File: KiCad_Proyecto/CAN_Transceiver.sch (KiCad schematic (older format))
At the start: 24 parts, among them Q6 2N7002, U4 MCP25612FD, U5 TH8056, U6 PESD1CAN, U7 PESD1CAN, U8 PESD1CAN

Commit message: todos los .sch arreglados
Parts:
- C16, C17, C18, C19, C20, C21, C22, C23: symbol PF_apiner-rescue:C-OBDII_IoT1 -> OBDII_IoT:C
- Q6: symbol PF_apiner-rescue:MOS_N-OBDII_IoT1 -> OBDII_IoT:MOS_N
- R15, R16, R17, R18, R19, R20, R21, R22, R23, R24: symbol PF_apiner-rescue:R-OBDII_IoT1 -> OBDII_IoT:R
- U4: symbol PF_apiner-rescue:MCP25612FD-OBDII_IoT1 -> OBDII_IoT:MCP25612FD
- U5: symbol PF_apiner-rescue:TH8056-OBDII_IoT1 -> OBDII_IoT:TH8056
- U6, U7, U8: symbol PF_apiner-rescue:PESD1CAN-OBDII_IoT1 -> OBDII_IoT:PESD1CAN
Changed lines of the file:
@@
 EESchema Schematic File Version 4
 LIBS:PF_apiner-cache
-EELAYER 29 0
+EELAYER 26 0
 EELAYER END
 $Descr A4 11693 8268
@@
 HS_CAN_RX
 $Comp
-L PF_apiner-rescue:PESD1CAN-OBDII_IoT1 U6
+L OBDII_IoT:PESD1CAN U6
 U 1 1 582F34D6
 P 5300 6250
@@
 $EndComp
 $Comp
-L PF_apiner-rescue:GND-OBDII_IoT1 #PWR060
+L OBDII_IoT:GND #PWR060
 U 1 1 582F433E
 P 5300 6700
@@
 $EndComp
 $Comp
-L PF_apiner-rescue:R-OBDII_IoT1 R21
+L OBDII_IoT:R R21
 U 1 1 58B0A852
 P 5750 5100
@@
 $EndComp
 $Comp
-L PF_apiner-rescue:MCP25612FD-OBDII_IoT1 U4
+L OBDII_IoT:MCP25612FD U4
 U 1 1 58EEA34D
 P 3450 5150
@@
 $EndComp
 $Comp
-L PF_apiner-rescue:TH8056-OBDII_IoT1 U5
+L OBDII_IoT:TH8056 U5
 U 1 1 58F03C6E
 P 3700 2950
@@
 SW_CAN_LOAD
 $Comp
-L PF_apiner-rescue:+5V_SW-OBDII_IoT1 #PWR061
+L OBDII_IoT:+5V_SW #PWR061
 U 1 1 58FD2521
 P 3150 5100
@@
 $EndComp
 $Comp
-L PF_apiner-rescue:PESD1CAN-OBDII_IoT1 U7
+L OBDII_IoT:PESD1CAN U7
 U 1 1 58FD2706
 P 6000 3650
@@
 $EndComp
 $Comp
-L PF_apiner-rescue:GND-OBDII_IoT1 #PWR062
+L OBDII_IoT:GND #PWR062
 U 1 1 58FD270C
 P 6000 4050
@@
 $EndComp
 $Comp
-L PF_apiner-rescue:R-OBDII_IoT1 R17
+L OBDII_IoT:R R17
 U 1 1 58FD347C
 P 4600 6100
@@
 $EndComp
 $Comp
-L PF_apiner-rescue:C-OBDII_IoT1 C19
+L OBDII_IoT:C C19
 U 1 1 58FD3B6F
 P 4600 6450
@@
 $EndComp
 $Comp
-L PF_apiner-rescue:R-OBDII_IoT1 R19
+L OBDII_IoT:R R19
 U 1 1 58FD3FA7
 P 4900 6100
@@
 $EndComp
 $Comp
-L PF_apiner-rescue:C-OBDII_IoT1 C20
+L OBDII_IoT:C C20
 U 1 1 58FD3FB1
 P 4900 6450
@@
 $EndComp
 $Comp
-L PF_apiner-rescue:PESD1CAN-OBDII_IoT1 U8
+L OBDII_IoT:PESD1CAN U8
 U 1 1 58FD4234
 P 6450 6250
@@
 $EndComp
 $Comp
-L PF_apiner-rescue:GND-OBDII_IoT1 #PWR063
+L OBDII_IoT:GND #PWR063
 U 1 1 58FD423A
 P 6450 6700
@@
 $EndComp
 $Comp
-L PF_apiner-rescue:R-OBDII_IoT1 R22
+L OBDII_IoT:R R22
 U 1 1 58FD4244
 P 5750 6100
@@
 $EndComp
 $Comp
-L PF_apiner-rescue:C-OBDII_IoT1 C22
+L OBDII_IoT:C C22
 U 1 1 58FD424E
 P 5750 6450
@@
 $EndComp
 $Comp
-L PF_apiner-rescue:R-OBDII_IoT1 R24
+L OBDII_IoT:R R24
 U 1 1 58FD4258
 P 6050 6100
@@
 $EndComp
 $Comp
-L PF_apiner-rescue:C-OBDII_IoT1 C23
+L OBDII_IoT:C C23
 U 1 1 58FD4262
 P 6050 6450
@@
 $EndComp
 $Comp
-L PF_apiner-rescue:GND-OBDII_IoT1 #PWR064
+L OBDII_IoT:GND #PWR064
 U 1 1 58FD430C
 P 4350 6700
@@
 $EndComp
 $Comp
-L PF_apiner-rescue:GND-OBDII_IoT1 #PWR065
+L OBDII_IoT:GND #PWR065
 U 1 1 58FD8A39
 P 4600 6700
@@
 $EndComp
 $Comp
-L PF_apiner-rescue:GND-OBDII_IoT1 #PWR066
+L OBDII_IoT:GND #PWR066
 U 1 1 58FD8A60
 P 4900 6700
@@
 $EndComp
 $Comp
-L PF_apiner-rescue:GND-OBDII_IoT1 #PWR067
+L OBDII_IoT:GND #PWR067
 U 1 1 58FD8B4B
 P 5750 6700
@@
 $EndComp
 $Comp
-L PF_apiner-rescue:GND-OBDII_IoT1 #PWR068
+L OBDII_IoT:GND #PWR068
 U 1 1 58FD8B72
 P 6050 6700
@@
 $EndComp
 $Comp
-L PF_apiner-rescue:GND-OBDII_IoT1 #PWR069
+L OBDII_IoT:GND #PWR069
 U 1 1 58FD9262
 P 2500 5700
@@
 $EndComp
 $Comp
-L PF_apiner-rescue:R-OBDII_IoT1 R23
+L OBDII_IoT:R R23
 U 1 1 58FDA2D5
 P 6050 5100
@@
 $EndComp
 $Comp
-L PF_apiner-rescue:C-OBDII_IoT1 C16
+L OBDII_IoT:C C16
 U 1 1 58FDBFE9
 P 2300 5250
@@
 $EndComp
 $Comp
-L PF_apiner-rescue:+5V_SW-OBDII_IoT1 #PWR070
+L OBDII_IoT:+5V_SW #PWR070
 U 1 1 58FDC0F6
 P 2100 5100
@@
 $EndComp
 $Comp
-L PF_apiner-rescue:C-OBDII_IoT1 C17
+L OBDII_IoT:C C17
 U 1 1 58FDC125
 P 2300 5550
@@
 $EndComp
 $Comp
-L PF_apiner-rescue:GND-OBDII_IoT1 #PWR071
+L OBDII_IoT:GND #PWR071
 U 1 1 58FDC707
 P 3200 6000
@@
 $EndComp
 $Comp
-L PF_apiner-rescue:+3.3V-OBDII_IoT1 #PWR072
+L OBDII_IoT:+3.3V #PWR072
 U 1 1 58FDF90E
 P 3200 2550
@@
 $EndComp
 $Comp
-L PF_apiner-rescue:DLC-OBDII_IoT1 #PWR073
+L OBDII_IoT:DLC #PWR073
 U 1 1 58FE3EFD
 P 4300 2550
@@
 $EndComp
 $Comp
-L PF_apiner-rescue:C-OBDII_IoT1 C18
+L OBDII_IoT:C C18
 U 1 1 58FE50CB
 P 4100 2600
@@
 $EndComp
 $Comp
-L PF_apiner-rescue:GND-OBDII_IoT1 #PWR074
+L OBDII_IoT:GND #PWR074
 U 1 1 58FE53E1
 P 3850 2650
@@
 	3850 2650 3850 2600
 $Comp
-L PF_apiner-rescue:MOS_N-OBDII_IoT1 Q6
+L OBDII_IoT:MOS_N Q6
 U 1 1 58FE7544
 P 5150 3650
@@
 $EndComp
 $Comp
-L PF_apiner-rescue:R-OBDII_IoT1 R16
+L OBDII_IoT:R R16
 U 1 1 58FE76BB
 P 4600 3250
@@
 $EndComp
 $Comp
-L PF_apiner-rescue:R-OBDII_IoT1 R20
+L OBDII_IoT:R R20
 U 1 1 58FE7CFE
 P 5250 3250
@@
 $EndComp
 $Comp
-L PF_apiner-rescue:R-OBDII_IoT1 R18
+L OBDII_IoT:R R18
 U 1 1 58FEA340
 P 4900 3850
@@
 $EndComp
 $Comp
-L PF_apiner-rescue:GND-OBDII_IoT1 #PWR075
+L OBDII_IoT:GND #PWR075
 U 1 1 58FEA42D
 P 5250 4050
@@
 $EndComp
 $Comp
-L PF_apiner-rescue:C-OBDII_IoT1 C21
+L OBDII_IoT:C C21
 U 1 1 58FEA778
 P 5550 3550
@@
 $EndComp
 $Comp
-L PF_apiner-rescue:GND-OBDII_IoT1 #PWR076
+L OBDII_IoT:GND #PWR076
 U 1 1 58FEAC5F
 P 4300 4050
@@
 	5250 3450 5250 3400
 $Comp
-L PF_apiner-rescue:GND-OBDII_IoT1 #PWR077
+L OBDII_IoT:GND #PWR077
 U 1 1 58FEBC1A
 P 5550 4050
@@
 	6000 4000 6000 4050
 $Comp
-L PF_apiner-rescue:R-OBDII_IoT1 R15
+L OBDII_IoT:R R15
 U 1 1 58FE8C9D
 P 3200 2750

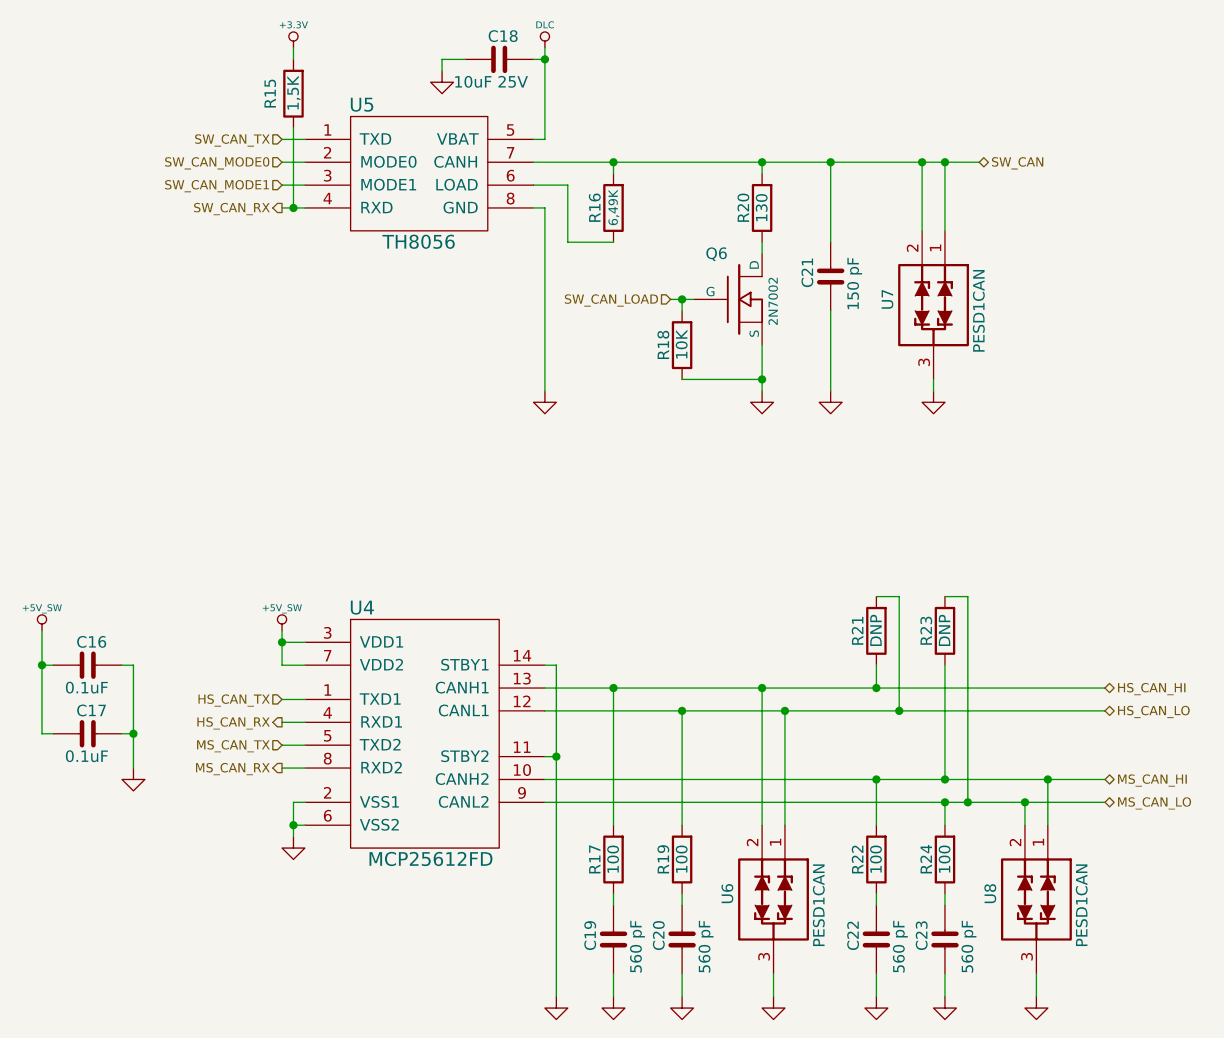
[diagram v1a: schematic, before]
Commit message: agregado valor a la R
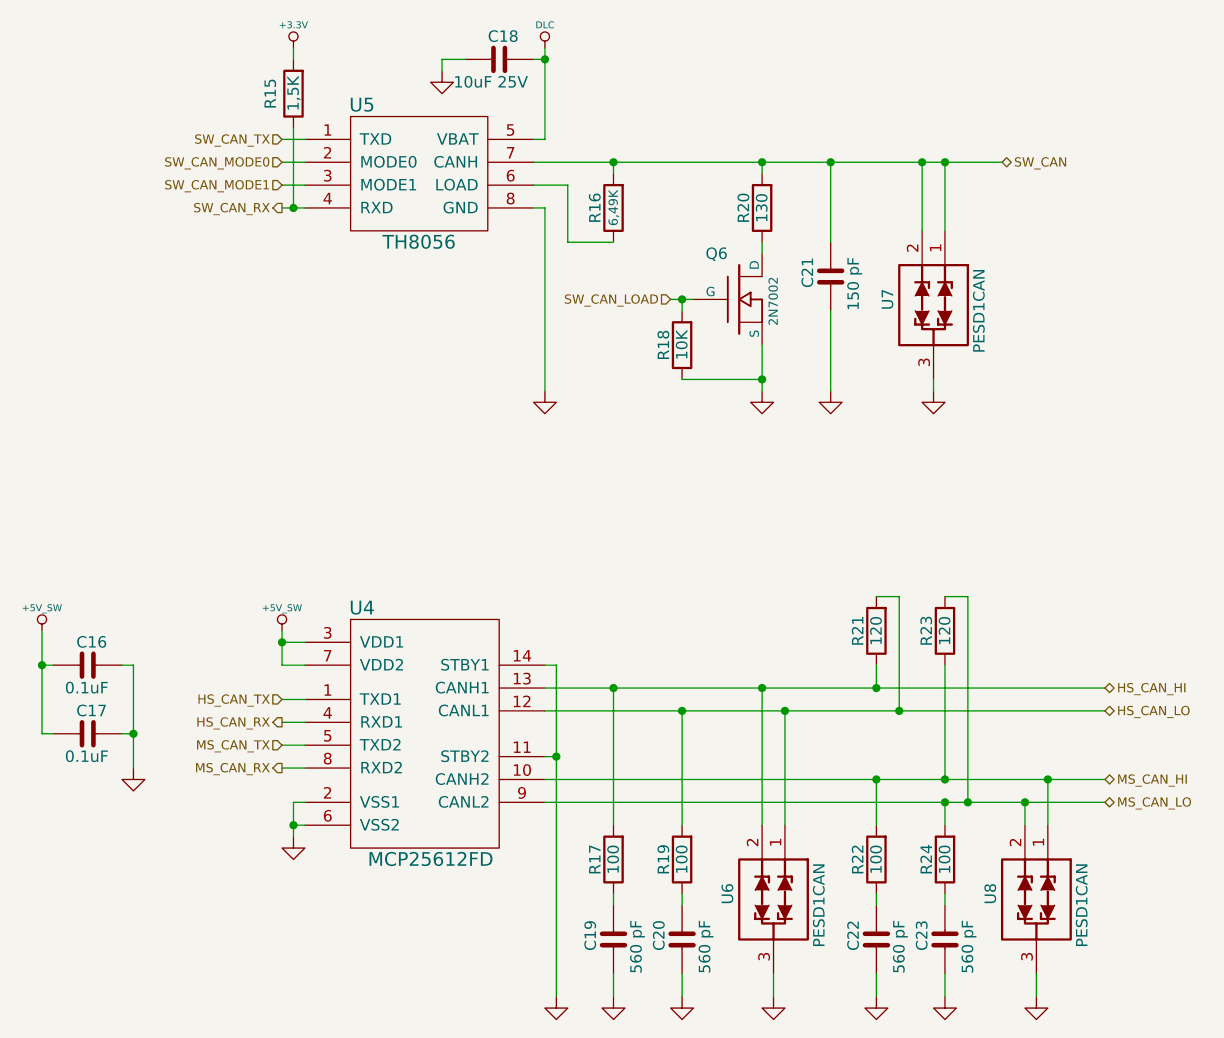
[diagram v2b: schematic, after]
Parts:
- R21, R23: value DNP -> 120
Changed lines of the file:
@@
 P 5750 5100
 F 0 "R21" V 5830 5100 50  0000 C CNN
-F 1 "DNP" V 5750 5100 50  0000 C CNN
+F 1 "120" V 5750 5100 50  0000 C CNN
 F 2 "chip_rlc:c_0402" V 5680 5100 50  0001 C CNN
 F 3 "" H 5750 5100 50  0000 C CNN
@@
 Text HLabel 6750 5450 2    40   BiDi ~ 0
 HS_CAN_LO
-Text HLabel 6200 3050 2    40   BiDi ~ 0
+Text HLabel 6300 3050 2    40   BiDi ~ 0
 SW_CAN
 Text HLabel 3150 5600 0    40   Input ~ 0
@@
 P 6050 5100
 F 0 "R23" V 6130 5100 50  0000 C CNN
-F 1 "DNP" V 6050 5100 50  0000 C CNN
+F 1 "120" V 6050 5100 50  0000 C CNN
 F 2 "chip_rlc:c_0402" V 5980 5100 50  0001 C CNN
 F 3 "" H 6050 5100 50  0000 C CNN
@@
 	4300 5250 4350 5250
 Wire Wire Line
-	4350 5250 4350 6700
+	4350 5250 4350 5650
 Wire Wire Line
 	4300 5650 4350 5650
 Connection ~ 4350 5650
 Wire Wire Line
-	4300 5350 6750 5350
-Wire Wire Line
-	4300 5450 6750 5450
+	4300 5350 4600 5350
+Wire Wire Line
+	4300 5450 4900 5450
 Wire Wire Line
 	6450 6700 6450 6600
@@
 	4600 6700 4600 6600
 Wire Wire Line
-	4300 5750 6750 5750
-Wire Wire Line
-	4300 5850 6750 5850
+	4300 5750 5750 5750
+Wire Wire Line
+	4300 5850 6050 5850
 Wire Wire Line
 	4600 5950 4600 5350
@@
 	3150 5250 3250 5250
 Wire Wire Line
-	3150 5100 3150 5250
+	3150 5100 3150 5150
 Wire Wire Line
 	3250 5150 3150 5150
@@
 Connection ~ 6150 5850
 Wire Wire Line
-	2500 5250 2500 5700
+	2500 5250 2500 5550
 Wire Wire Line
 	2500 5250 2450 5250
@@
 	2100 5550 2150 5550
 Wire Wire Line
-	2100 5100 2100 5550
+	2100 5100 2100 5250
 Wire Wire Line
 	2150 5250 2100 5250
 Connection ~ 2100 5250
 Wire Wire Line
-	3200 5850 3200 6000
+	3200 5850 3200 5950
 Wire Wire Line
 	3200 5850 3250 5850
@@
 Connection ~ 3200 5950
 Wire Wire Line
-	3150 3250 3250 3250
+	3150 3250 3200 3250
 Wire Wire Line
 	3150 3150 3250 3150
@@
 Connection ~ 3200 3250
 Wire Wire Line
-	4300 2550 4300 2950
+	4300 2550 4300 2600
 Wire Wire Line
 	4300 2950 4250 2950
@@
 $EndComp
 Wire Wire Line
-	5250 3850 5250 4050
+	5250 3850 5250 4000
 Wire Wire Line
 	4900 4000 5250 4000
 Connection ~ 5250 4000
 Wire Wire Line
-	4850 3650 4950 3650
+	4850 3650 4900 3650
 Wire Wire Line
 	4900 3700 4900 3650
 Connection ~ 4900 3650
 Wire Wire Line
-	4250 3050 6200 3050
+	4250 3050 4600 3050
 Wire Wire Line
 	4250 3150 4400 3150
@@
 	6400 5950 6400 5850
 Connection ~ 6400 5850
+Wire Wire Line
+	4350 5650 4350 6700
+Wire Wire Line
+	4600 5350 5250 5350
+Wire Wire Line
+	4900 5450 5350 5450
+Wire Wire Line
+	5250 5350 5750 5350
+Wire Wire Line
+	5350 5450 5850 5450
+Wire Wire Line
+	5750 5750 6050 5750
+Wire Wire Line
+	6050 5850 6150 5850
+Wire Wire Line
+	3150 5150 3150 5250
+Wire Wire Line
+	5750 5350 6750 5350
+Wire Wire Line
+	5850 5450 6750 5450
+Wire Wire Line
+	6050 5750 6500 5750
+Wire Wire Line
+	6150 5850 6400 5850
+Wire Wire Line
+	2500 5550 2500 5700
+Wire Wire Line
+	2100 5250 2100 5550
+Wire Wire Line
+	3200 5950 3200 6000
+Wire Wire Line
+	3200 3250 3250 3250
+Wire Wire Line
+	4300 2600 4300 2950
+Wire Wire Line
+	5250 4000 5250 4050
+Wire Wire Line
+	4900 3650 4950 3650
+Wire Wire Line
+	4600 3050 5250 3050
+Wire Wire Line
+	5250 3050 5550 3050
+Wire Wire Line
+	5550 3050 5950 3050
+Wire Wire Line
+	5950 3050 6050 3050
+Wire Wire Line
+	6500 5750 6750 5750
+Wire Wire Line
+	6400 5850 6750 5850
+Wire Wire Line
+	6050 3050 6300 3050
 $EndSCHEMATC
